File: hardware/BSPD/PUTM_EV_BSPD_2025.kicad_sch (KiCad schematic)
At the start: 36 parts, among them J1 BS2, J2 BS1, J3 CS, K2 TE AXICOM IM07DTS, Q1 BS170F, U10 LM393B, U11 74HC1G08GV, U3 NE555DR, U5 74HC1G08GV, U6 74HC3G14

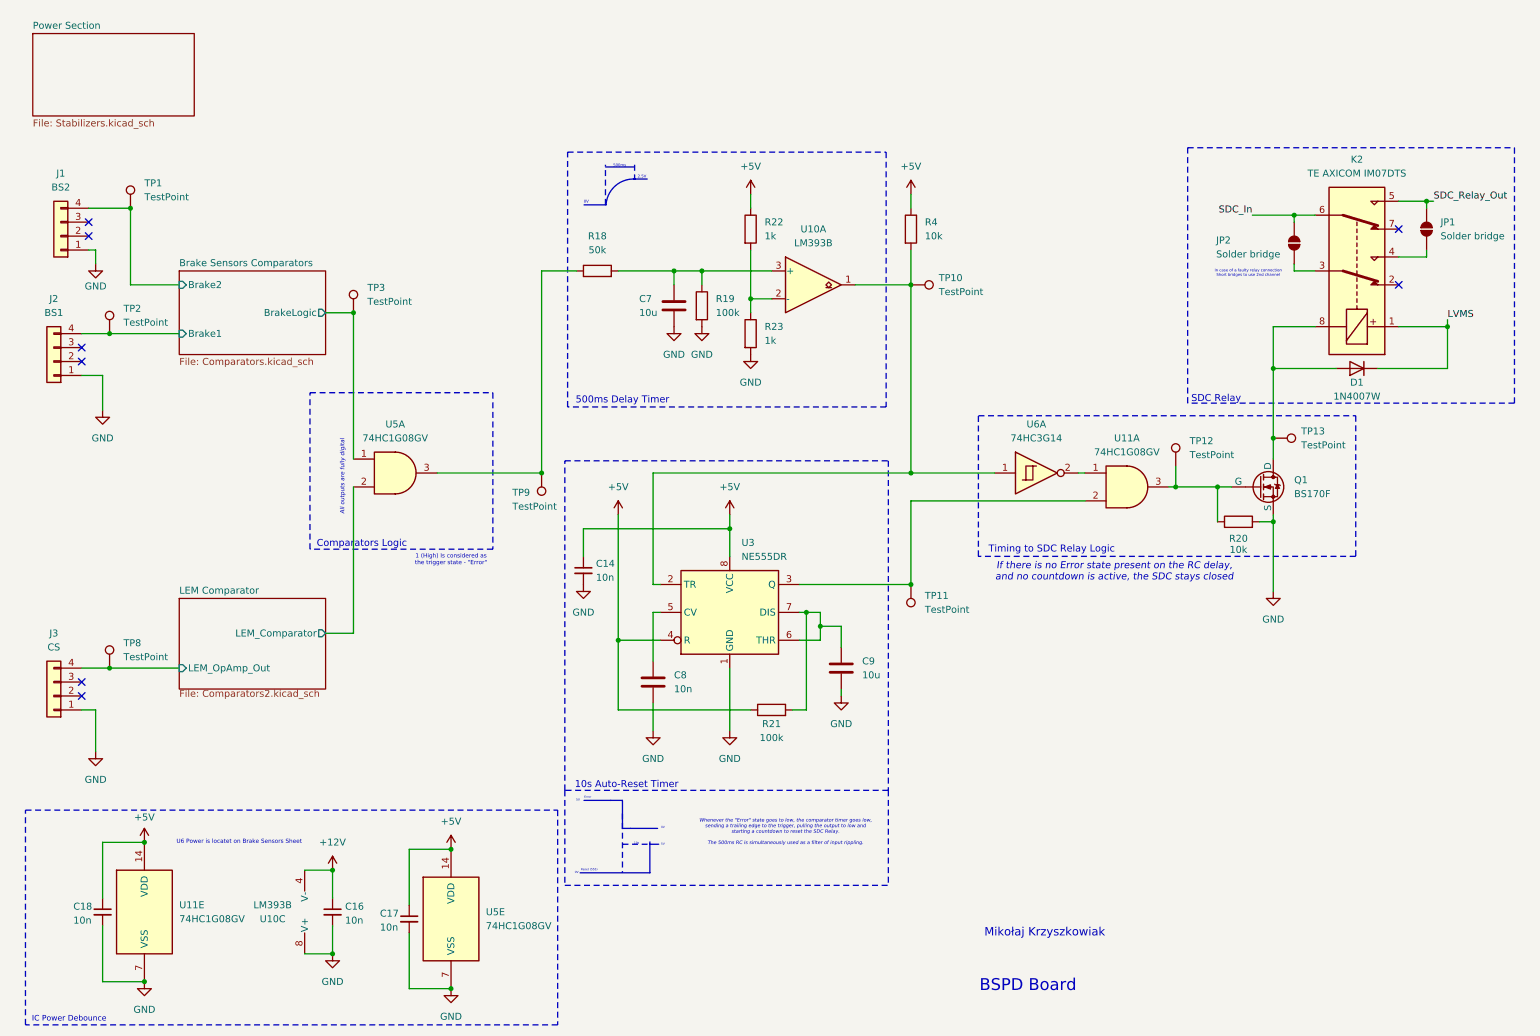
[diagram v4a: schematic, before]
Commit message: Fixed 555 configuration + power debouncing
Changed power debouncing capacitors to 100nF
Fixed the One-Shot 555
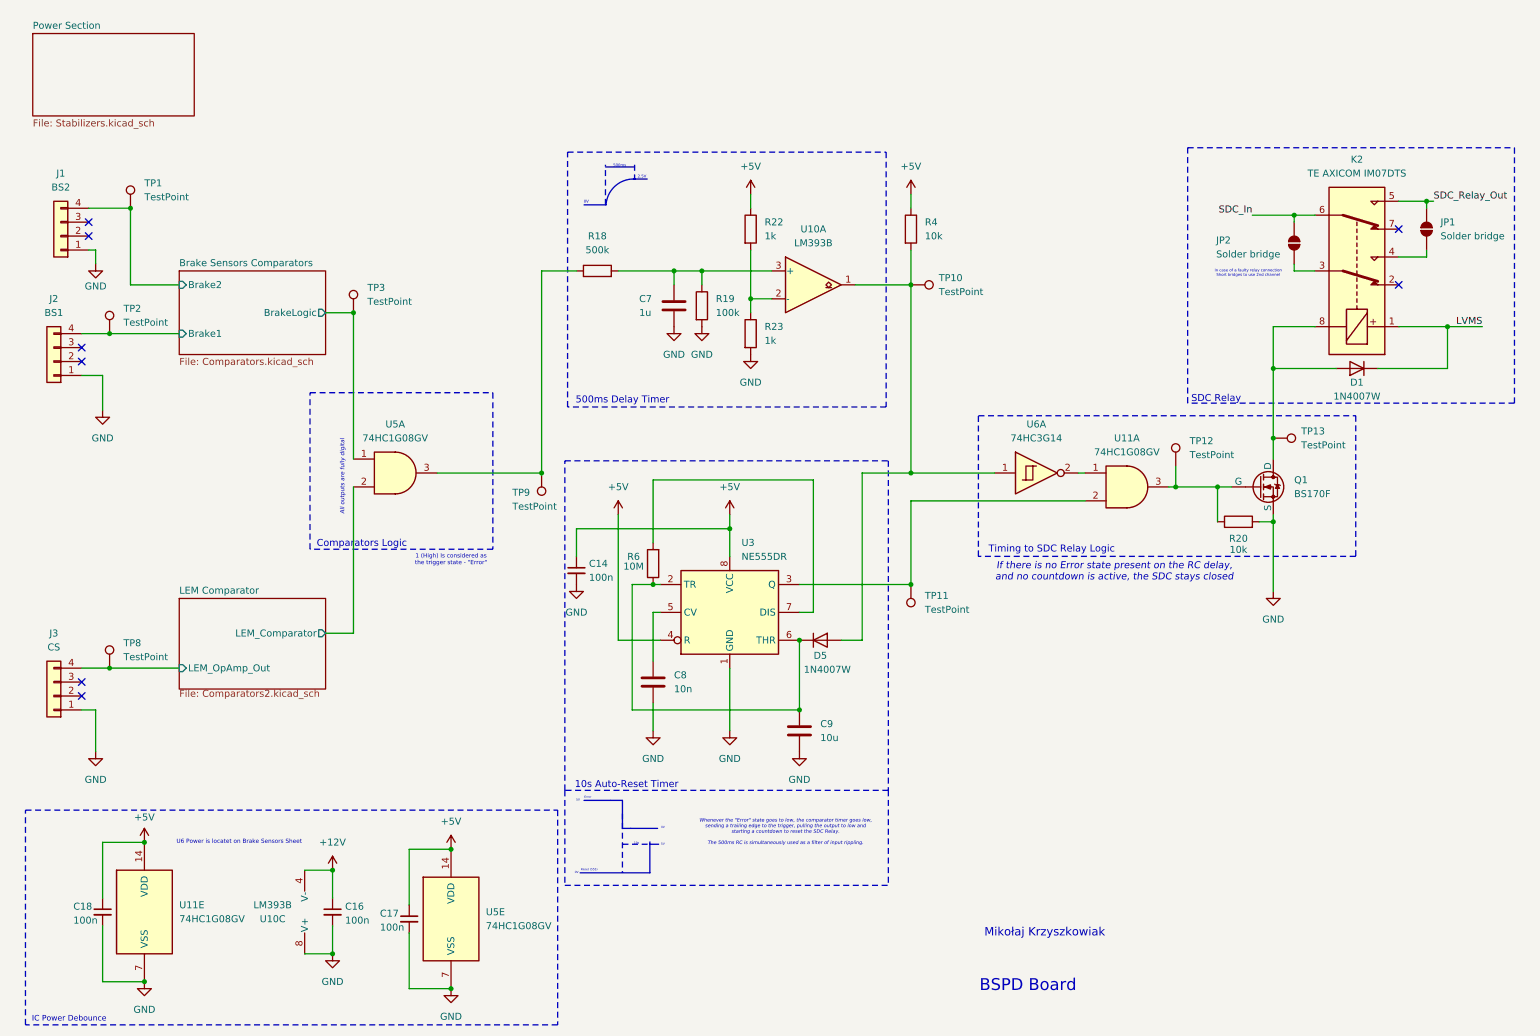
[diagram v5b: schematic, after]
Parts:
- removed R21: 100k, symbol Device:R
- added D5: 1N4007W, symbol Device:D
- added R6: 10M, symbol Device:R
- C14, C16, C17, C18: value 10n -> 100n
- C7: value 10u -> 1u
- R18: value 50k -> 500k
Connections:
- net at C9.1, U3.6 (THR): now also U3.2 (TR), D5.1 (K), R6.1; no longer U3.7 (DIS)
- net at R4.2, TP10.1, U10.1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: now also D5.2 (A); no longer U3.2 (TR)
- new net: R6.2, U3.7 (DIS)
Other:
- moved on the sheet: C14, C9

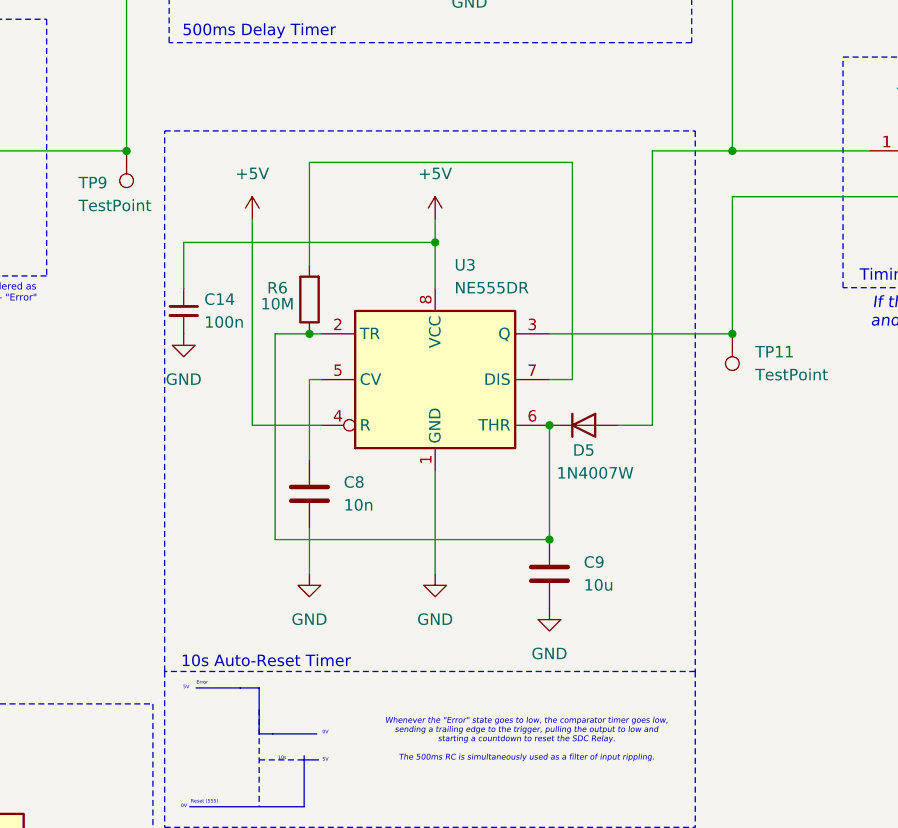
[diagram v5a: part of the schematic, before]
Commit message: Cleaned up messy 555 drawing
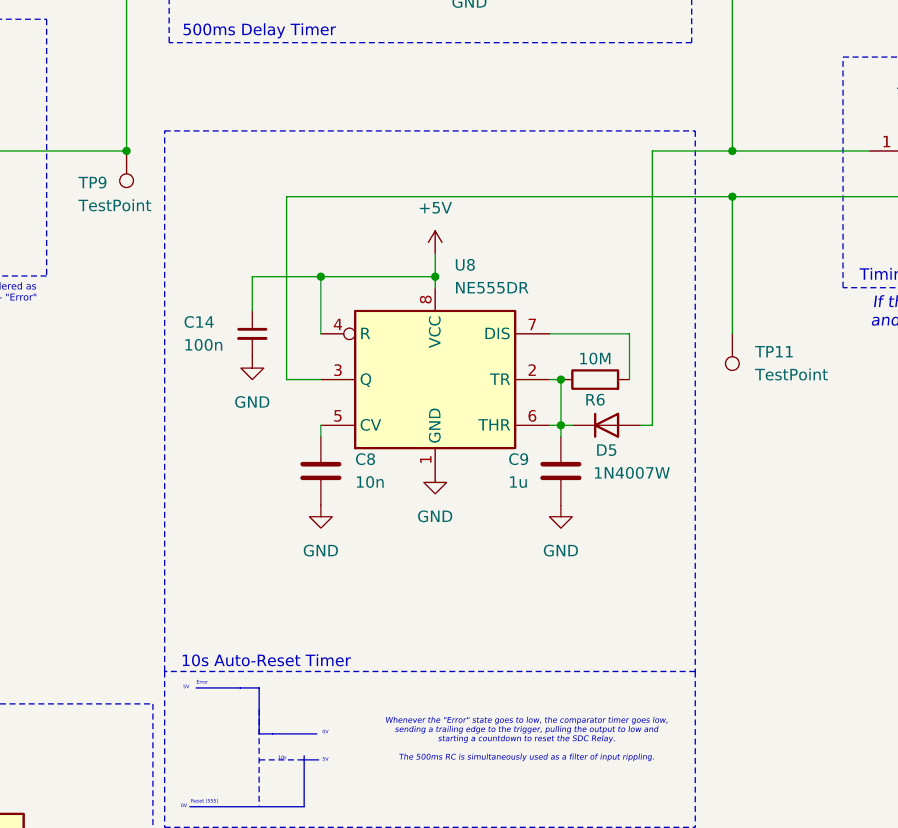
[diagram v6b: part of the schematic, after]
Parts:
- removed U3: NE555DR, Package_SO:SOIC-8_3.9x4.9mm_P1.27mm, symbol Timer:ICM7555xB
- added U8: NE555DR, Package_SO:SOIC-8_3.9x4.9mm_P1.27mm, symbol Timer:ICM7555xB
- C9: value 10u -> 1u
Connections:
- net +5V: now also U8.4 (R), U8.8 (VCC)
- net GND: now also U8.1 (GND)
- net at C9.1, D5.1 (K), R6.1: now also U8.2 (TR), U8.6 (THR)
- net at TP11.1, U11.2: now also U8.3 (Q)
- net at C8.1: now also U8.5 (CV)
- net at R6.2: now also U8.7 (DIS)
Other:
- moved on the sheet: C14, C8, C9, D5, R6

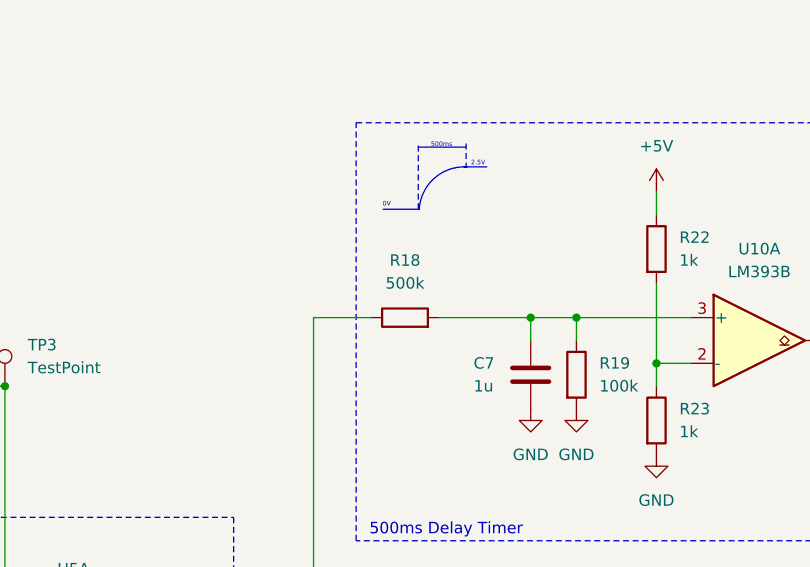
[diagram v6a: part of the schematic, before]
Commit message: Changed misassigner resistor value
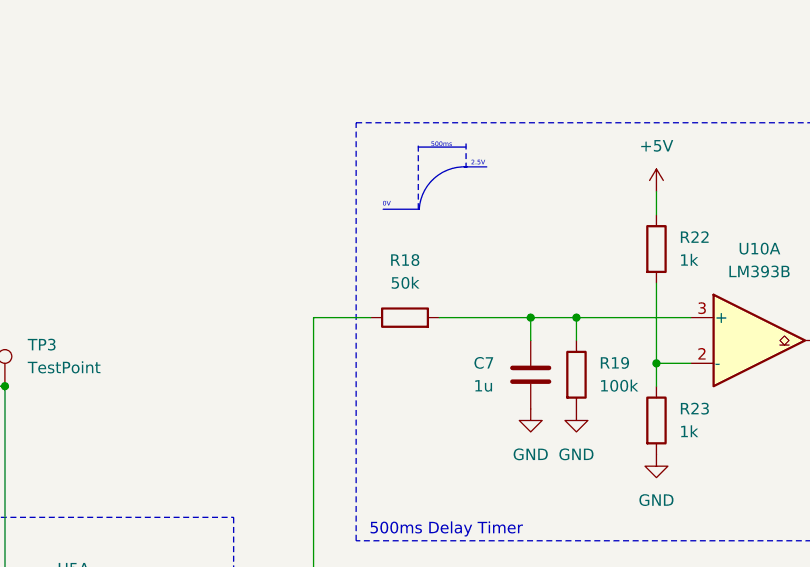
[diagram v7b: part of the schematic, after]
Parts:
- R18: value 500k -> 50k
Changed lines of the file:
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@@
 			)
 		)
-		(property "Value" "500k"
+		(property "Value" "50k"
 			(at 116.84 55.88 90)
 			(effects

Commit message: Fixed Comparators
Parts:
- D1: value 1N4007W -> SK36A-LTP
- D5: value 1N4007W -> NSVRB751V40T1G
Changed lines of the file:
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@@
 			)
 		)
-		(property "Value" "1N4007W"
-			(at 162.814 132.334 0)
-			(effects
-				(font
-					(size 1.27 1.27)
+		(property "Value" "NSVRB751V40T1G"
+			(at 163.068 131.318 0)
+			(effects
+				(font
+					(size 0.635 0.635)
 				)
 			)
@@
 			)
 		)
-		(property "Datasheet" "~"
+		(property "Datasheet" "https://eu.mouser.com/ProductDetail/onsemi/NSVRB751V40T1G?qs=dbuNSGnowt2jW1ha4241mA%3D%3D"
 			(at 160.02 127 0)
 			(effects
@@
 			)
 		)
-		(property "Value" "1N4007W"
+		(property "Value" "SK36A-LTP"
 			(at 255.27 82.55 0)
 			(effects
@@
 			)
 		)
-		(property "Datasheet" "https://eu.mouser.com/datasheet/2/345/1n4001w_1n4007w-2449105.pdf"
+		(property "Datasheet" "https://eu.mouser.com/ProductDetail/Micro-Commercial-Components-MCC/SK36A-LTP?qs=JeAkOuORR2UgZXSucJXzqg%3D%3D"
 			(at 255.27 77.47 0)
 			(effects
